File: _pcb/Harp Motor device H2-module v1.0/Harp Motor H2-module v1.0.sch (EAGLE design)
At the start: 70 parts, among them IC1 FT232RL, IC11 74LVC1G125DBV, IC12 74LVC1G125DBV, IC13 74LVC1G125DBV, IC3 LP5907MFX-3.3, IC7 USBLC6-2SC6, IC8 ATXMEGA32A4U, IC9 TLV70033DDCR, T1 DMG1012UW??, T2 DMG1012UW??, T3 DMG1012UW??, X1 USB_MINI_B, X2 Rot_Encoder, X3 EMRG_BUTT_IN_NO, X4 Hall_Effect, X7 STEP_MOTOR

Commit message: Harp Motor device H2-module v1.0; commit after revision
Harp Motor device H2-module v1.0:
- commit after revisions made with Filipe @Dezember 14th 2022
- missing components OEPS code & BOM
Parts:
- removed D4: BAT54, Harp Motor H2-module v1.0:BAT54
- removed IC13: 74LVC1G125DBV, Harp Motor H2-module v1.0:74LVC1G125DBV
- removed R10, R11: 0R, Harp Motor H2-module v1.0:R-US_R0402
- added C15: 4.7uF DNI, Harp Motor H2-module v1.0:C-EUC0603K
- added C16: 100nF, Harp Motor H2-module v1.0:C-EUC0402K
- added C41, C42: 15nF 5%, rcl:C-EUC0402
- added IC10: OPA365, CNP-ics 2:OPA365
- added L3: 40R@100MHz, Harp Motor H2-module v1.0:R-EU_R0805
- added R14, R15, R16: DNI, Harp Motor H2-module v1.0:R-US_R0402
- added R17, R19: 10k 1%, rcl:R-EU_R0402
- added R20: 24k, rcl:R-EU_R0402
- added R21: 15k, rcl:R-EU_R0402
- added R9: 100R DNI, Harp Motor H2-module v1.0:R-US_R0402
- L1, L2: device Harp Motor H2-module v1.0:R-EU_R0603 -> Harp Motor H2-module v1.0:R-EU_R0805
- R4: value 0R -> 0R DNI
- R7: value 10k -> 10k DNI
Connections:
- removed net N$59: IC8.PC4/OC1A/!SS, R10.1
- removed net N$60: IC8.PC3/OC0D/TXD0, R11.1
- new net N$50: C41.2, R17.2, R19.1
- new net N$62: C15.1, R4.2, R9.1
- new net N$63: C16.1, IC8.AVCC, L3.1
- new net N$64: IC10.-IN, IC10.OUT, R17.1
- new net N$65: IC10.+IN, R20.1, R21.2
- net +3V3: now also IC10.V+; no longer IC13.VCC
- net +3V3_U: now also L3.2, R9.2; no longer IC8.AVCC, R4.2
- net +5V: now also R14.2, R15.2, R16.2
- net CLOCK_IN: now also IC8.PC2/OC0C/RXD0; no longer IC8.PB1/ADC9
- net GND: now also C15.2, C16.2, C41.1, C42.1, IC10.V-, IC8.PA2/ADC2, R21.1; no longer IC13.GND, IC13.OE
- net HALL_EFFCT_IN: now also R20.2; no longer IC13.I
- net STEP_DIRECTION: now also R15.1
- net STEP_ENABLE: now also R16.1
- net STEP_PULSE: now also R14.1
- net U_ENCODER_A_PHASE: now also IC8.PC5/OC1B/MOSI/XCK1; no longer R10.2
- net U_ENCODER_B_PHASE: now also IC8.PC4/OC1A/!SS; no longer R11.2
- net U_HALL_EFFCT_IN: now also C42.2, R19.2; no longer IC13.O
- net U_STEP_ENABLE: now also IC8.PC3/OC0D/TXD0; no longer IC8.PC5/OC1B/MOSI/XCK1
- net U_STEP_PULSE: now also IC8.PC0/OC0A/SDA; no longer IC8.PC7/SCK/TXD1/CLKO/EVO
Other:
- note added: "2nd Order LPF: 1.061 kHz"
- note removed: "BNCs output: needed?? connected to two Teensy DAC Stage rotation signal ?? (be sure about) maybe only auxiliary IO.."
- note removed: "Camera Controller - Clock_IN: PC2 H1 tb mesmo pino?? - interrupst (?): PC0 PD0 - analog IN: ?? - camera Strobes (Interrupts?): CAM0: PA0=Strobe & PA1=PullUp CAM1: PD6=PullUp & PD7=Strobe"
- note removed: "check ferrite case"
- note removed: "check pinout not as in abstarct draw"
- note removed: "confirmar encoder A & B phase: OC0A & OC0B"
- note removed: "input missing?? Treadmill Motion?? what have to do about it?"
- note removed: "pinout order: same as sensor"
- moved on the sheet: C1, L2, X4-1, X4-2, X4-3

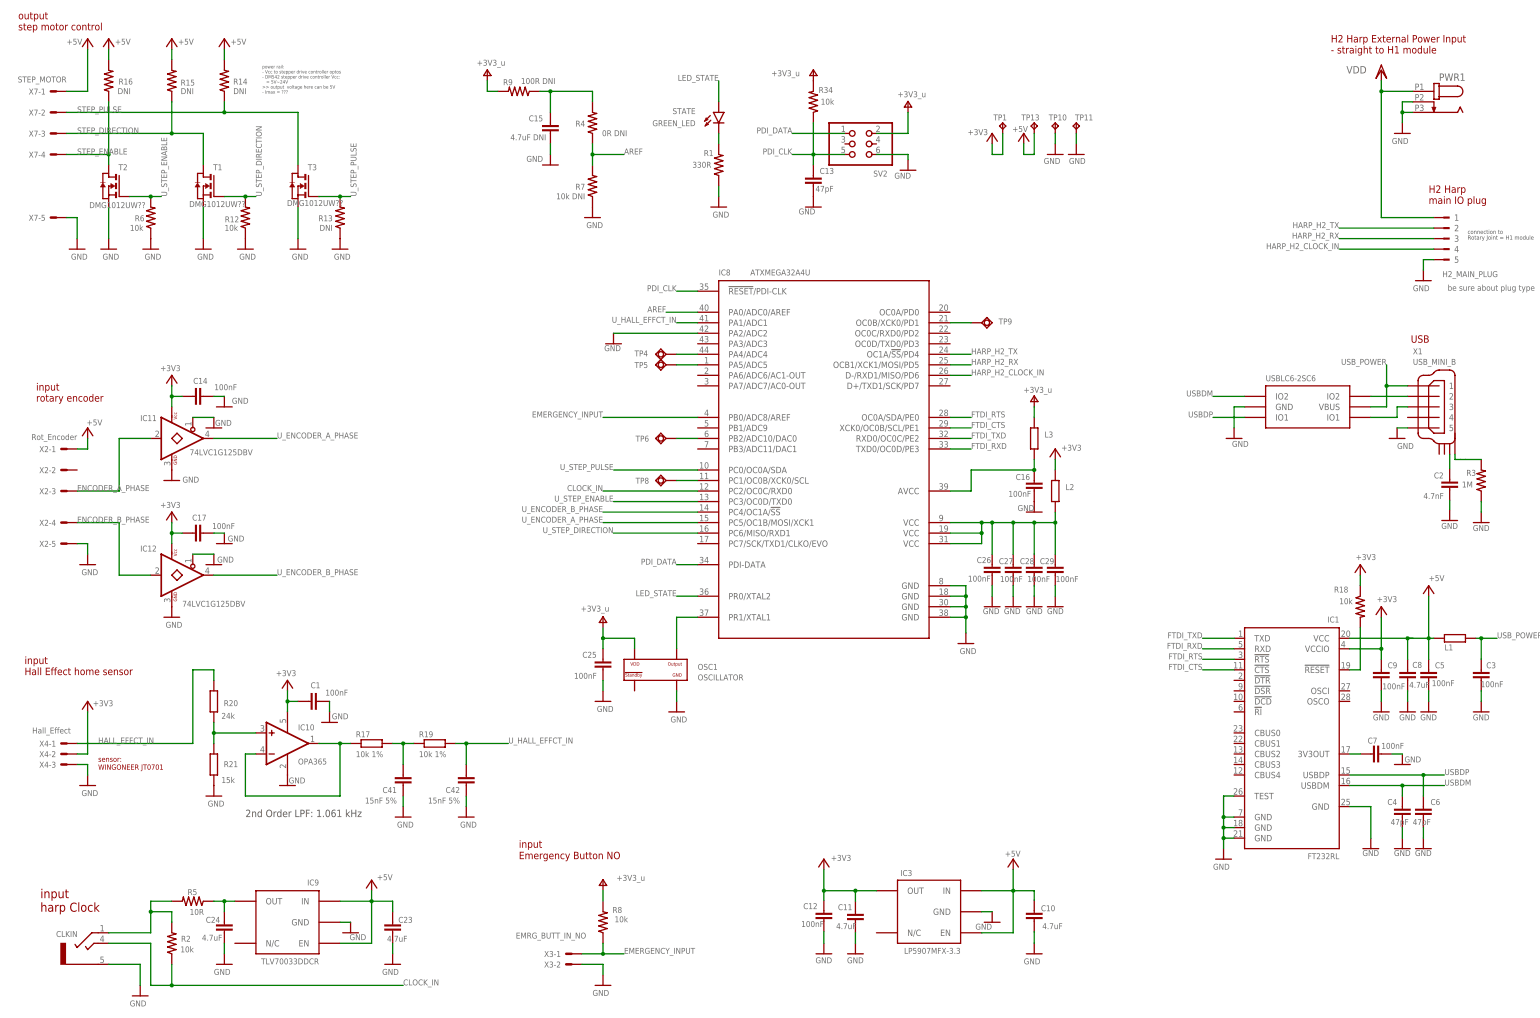
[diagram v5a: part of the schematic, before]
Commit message: Harp Motor device H2-module v1.0 - last revision with Filipe
- extra R0 on some stages
- IO headers - GND pin was on wrong end
- rebuild user-friend labelling

- still missing OEPS components code & BOM
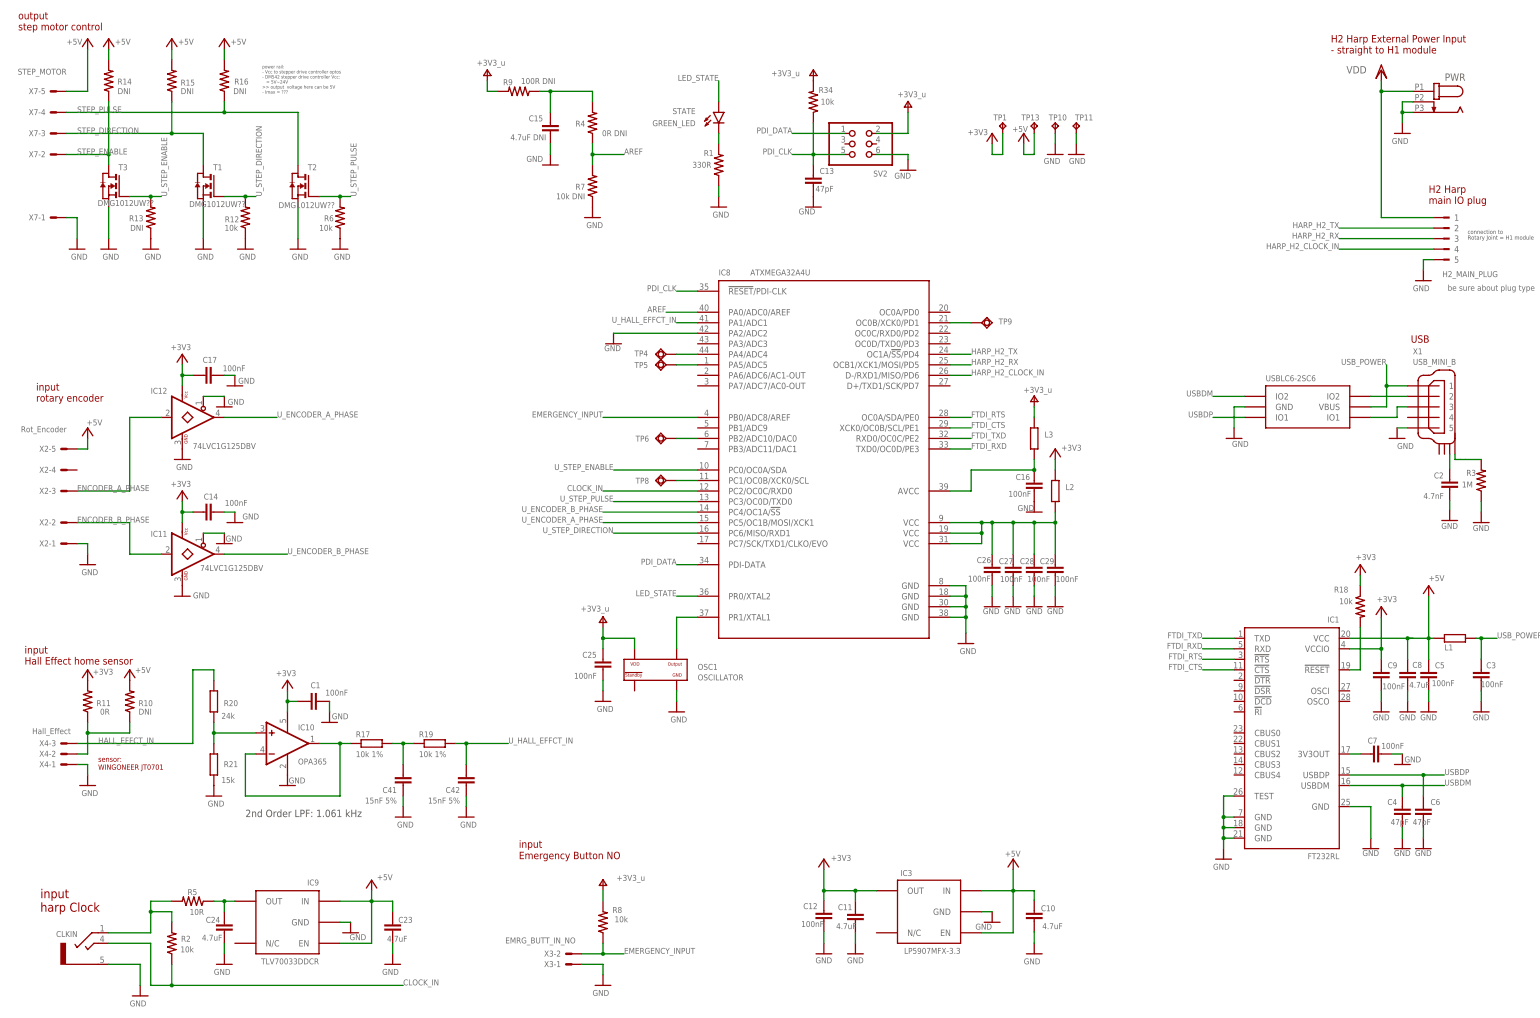
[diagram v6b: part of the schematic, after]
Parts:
- added R10: DNI, Harp Motor H2-module v1.0:R-US_R0402
- added R11: 0R, Harp Motor H2-module v1.0:R-US_R0402
- renumbered PWR1 to PWR
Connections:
- new net N$51: R10.1, R11.1, X4-2.S
- net +3V3: now also R11.2; no longer X4-2.S
- net +5V: now also R10.2, X2-5.S, X7-5.S; no longer X2-1.S, X7-1.S
- net EMERGENCY_INPUT: now also X3-2.S; no longer X3-1.S
- net ENCODER_A_PHASE: now also IC12.I; no longer IC11.I
- net ENCODER_B_PHASE: now also IC11.I, X2-2.S; no longer IC12.I, X2-4.S
- net GND: now also X2-1.S, X3-1.S, X4-1.S, X7-1.S; no longer X2-5.S, X3-2.S, X4-3.S, X7-5.S
- net HALL_EFFCT_IN: now also X4-3.S; no longer X4-1.S
- net STEP_ENABLE: now also R14.1, T3.D, X7-2.S; no longer R16.1, T2.D, X7-4.S
- net STEP_PULSE: now also R16.1, T2.D, X7-4.S; no longer R14.1, T3.D, X7-2.S
- net U_ENCODER_A_PHASE: now also IC12.O; no longer IC11.O
- net U_ENCODER_B_PHASE: now also IC11.O; no longer IC12.O
- net U_STEP_ENABLE: now also IC8.PC0/OC0A/SDA, R13.2, T3.G; no longer IC8.PC3/OC0D/TXD0, R6.2, T2.G
- net U_STEP_PULSE: now also IC8.PC3/OC0D/TXD0, R6.2, T2.G; no longer IC8.PC0/OC0A/SDA, R13.2, T3.G
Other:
- moved on the sheet: C14, C17, IC11, IC12, R13, R14, R16, R6, T2, T3, X2-1, X2-2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

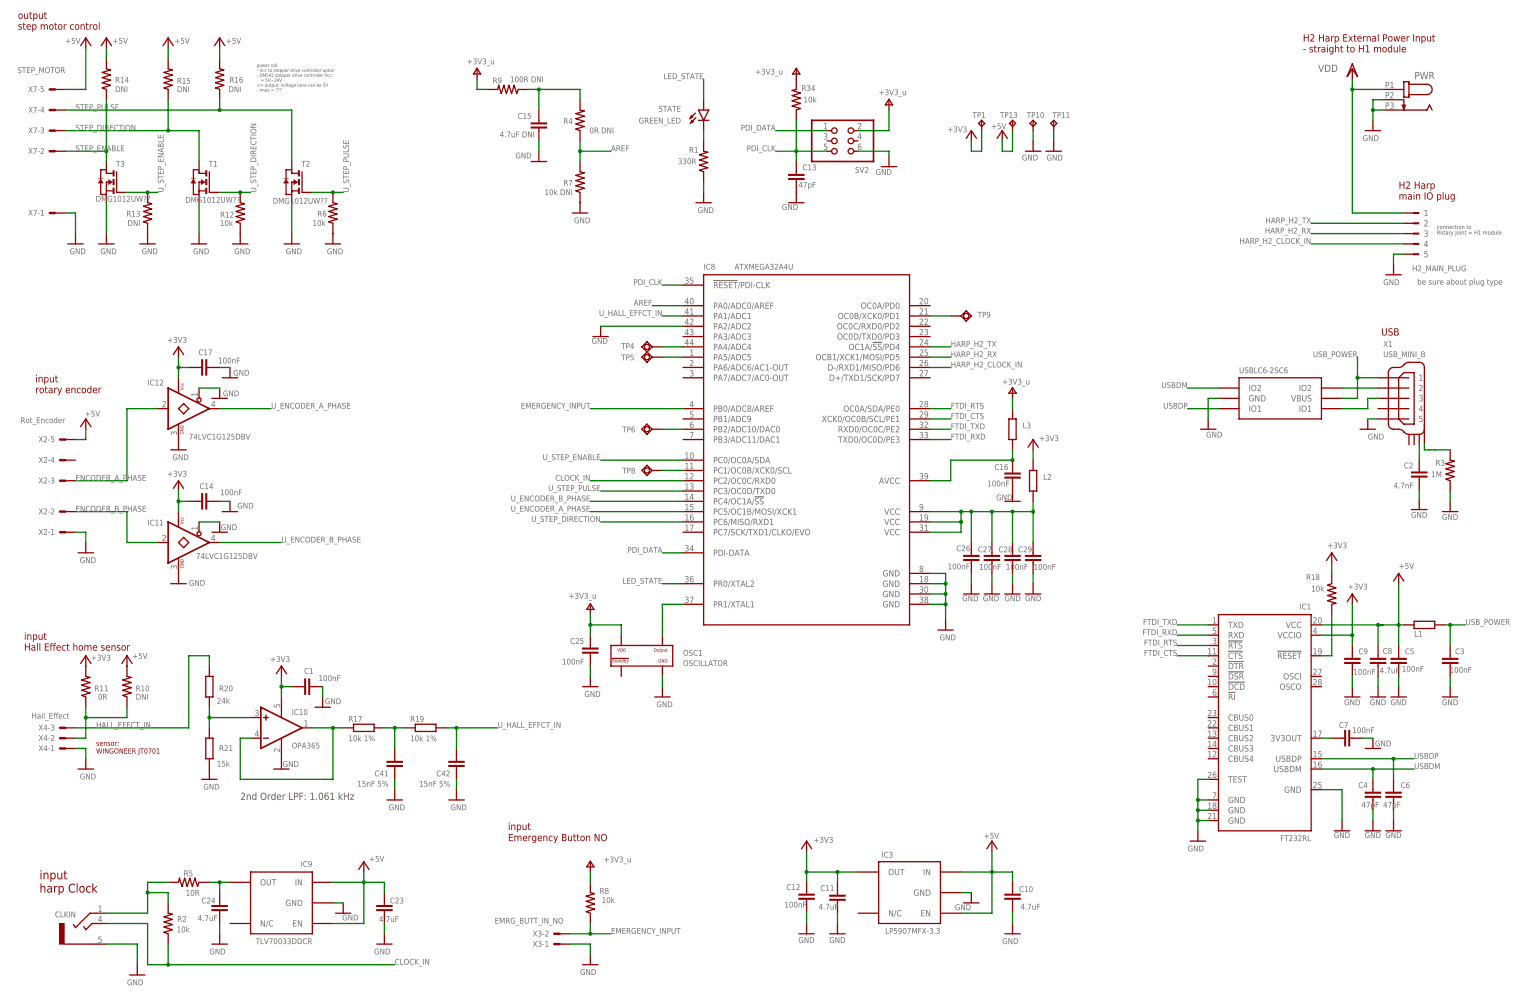
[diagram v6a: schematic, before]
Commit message: Harp Motor device H2-module v1.0 - final changes
Harp Motor device H2-module v1.0 - final PCB changes
- labels sizes & positions modified
- removed clock conn from micro to main plug; added direct buffer from clock_in to main harp plug;
- corrected Harp_Tx & Harp_Rx pins
- still missing BOM & OEPS components codes
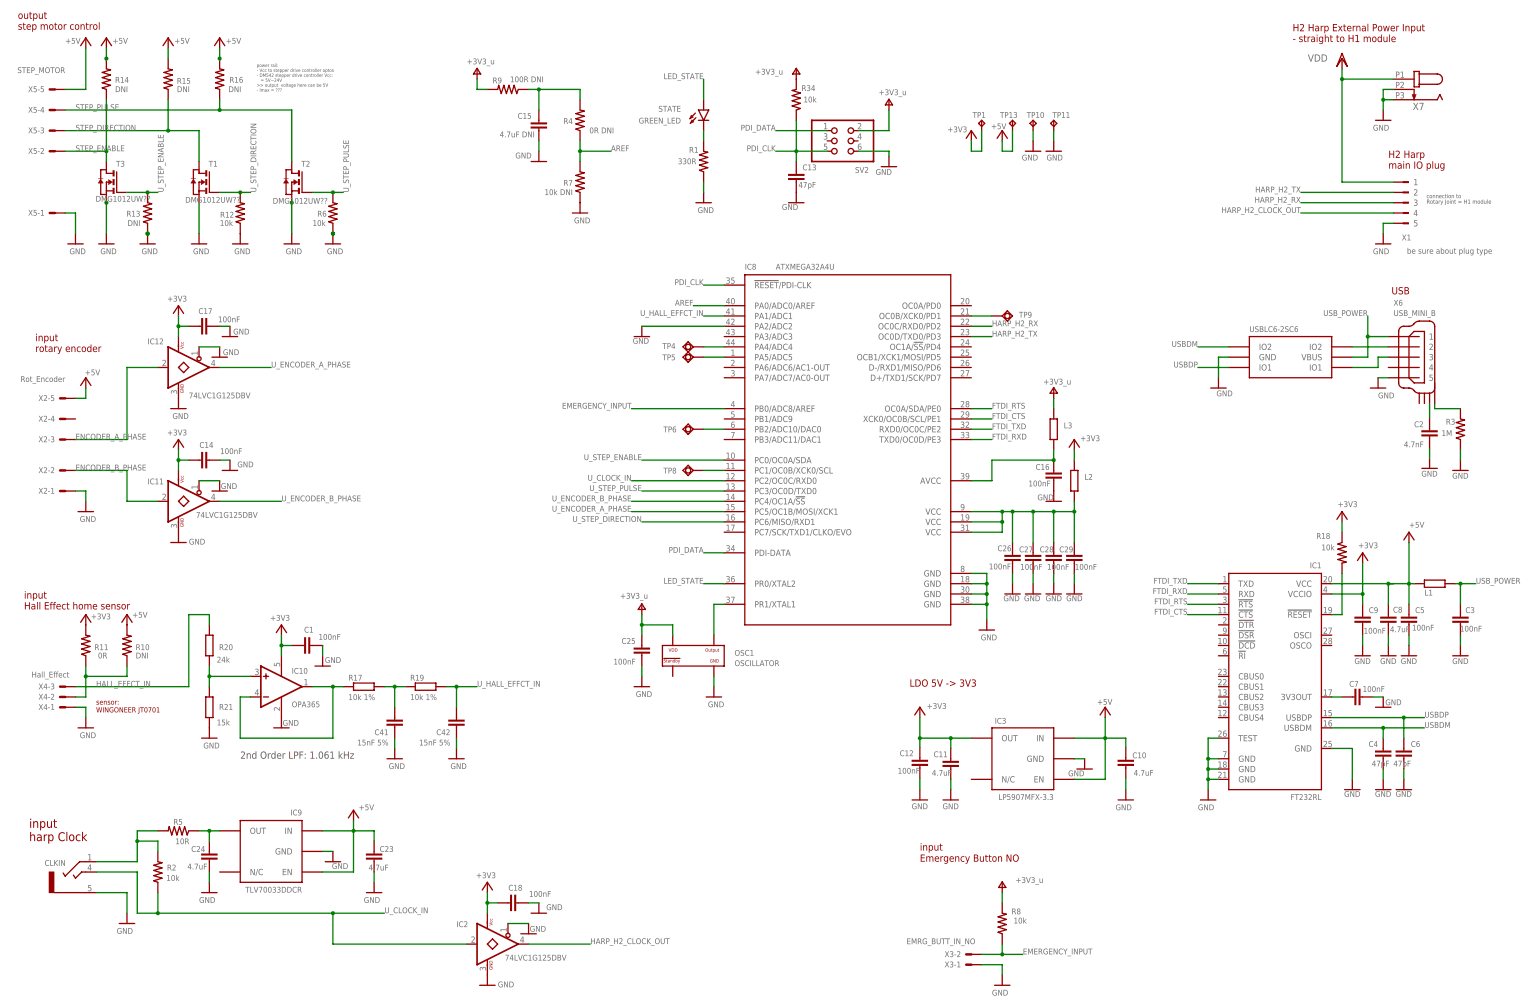
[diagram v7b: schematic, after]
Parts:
- removed H2_MAIN_PLUG: be sure about plug type, Harp Motor H2-module v1.0:90G-5
- removed PWR: DC_JACK2.1MM, harp camera controller:DC_JACK2.1MM
- added C18: 100nF, Harp Motor H2-module v1.0:C-EUC0402K
- added IC2: 74LVC1G125DBV, Harp Motor H2-module v1.0:74LVC1G125DBV
- added X5: STEP_MOTOR, Harp Motor H2-module v1.0:22-23-2051
- added X6: USB_MINI_B, VestibularVR H1-module v1.0:USB_MINI_B
- X1: value USB_MINI_B -> be sure about plug type; device VestibularVR H1-module v1.0:USB_MINI_B -> Harp Motor H2-module v1.0:90G-5; MPN UX60-MB-5S8 -> 20.155MH/5-E; OEPS OEPS070021 -> OEPS070037
- X7: value STEP_MOTOR -> DC_JACK2.1MM; device Harp Motor H2-module v1.0:22-23-2051 -> harp camera controller:DC_JACK2.1MM; DIGIKEY_PN (none) -> DIGIKEY N.A.; MOUSER_PN (none) -> 163-179PH; MPN (none) -> 163-179PH-EX; NOTES (none) -> -; TYPE (none) -> TH
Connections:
- removed net CLOCK_IN: CLKIN.4, IC8.PC2/OC0C/RXD0, R2.1
- removed net HARP_H2_CLOCK_IN: H2_MAIN_PLUG.4, IC8.D-/RXD1/MISO/PD6
- new net HARP_H2_CLOCK_OUT: IC2.O, X1.4
- new net U_CLOCK_IN: CLKIN.4, IC2.I, IC8.PC2/OC0C/RXD0, R2.1
- net +3V3: now also C18.1, IC2.VCC
- net +5V: now also X5-5.S; no longer X7-5.S
- net GND: now also C18.2, IC2.GND, IC2.OE, X5-1.S, X6.5, X7.2, X7.3; no longer H2_MAIN_PLUG.5, PWR.2, PWR.3, X7-1.S
- net HARP_H2_RX: now also IC8.OC0C/RXD0/PD2, X1.3; no longer H2_MAIN_PLUG.3, IC8.OCB1/XCK1/MOSI/PD5
- net HARP_H2_TX: now also IC8.OC0D/TXD0/PD3, X1.2; no longer H2_MAIN_PLUG.2, IC8.OC1A/!SS!/PD4
- net N$1: now also X6.P$4; no longer X1.P$4
- net N$15: now also X6.P$3; no longer X1.P$3
- net N$2: now also X6.2; no longer X1.2
- net N$3: now also X6.3; no longer X1.3
- net STEP_DIRECTION: now also X5-3.S; no longer X7-3.S
- net STEP_ENABLE: now also X5-2.S; no longer X7-2.S
- net STEP_PULSE: now also X5-4.S; no longer X7-4.S
- net USB_POWER: now also X6.1; no longer X1.1
- net VDD: now also X1.1, X7.1; no longer H2_MAIN_PLUG.1, PWR.1
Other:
- note added: "LDO 5V -> 3V3"
- moved on the sheet: C1, C10, C11, C12, C14, C16, C17, C2, C23, C24, C25, C26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
